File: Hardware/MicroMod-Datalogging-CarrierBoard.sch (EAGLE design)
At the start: 75 parts, among them J11 microSD, J12 SPI, J14 I2C, J2 JTAG, J3 QWIIC_RIGHT_ANGLE, J5 UART, J6 MICROMOD-2222-C, J8 Dedicated, U1 3.3V, U2 MCP73831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

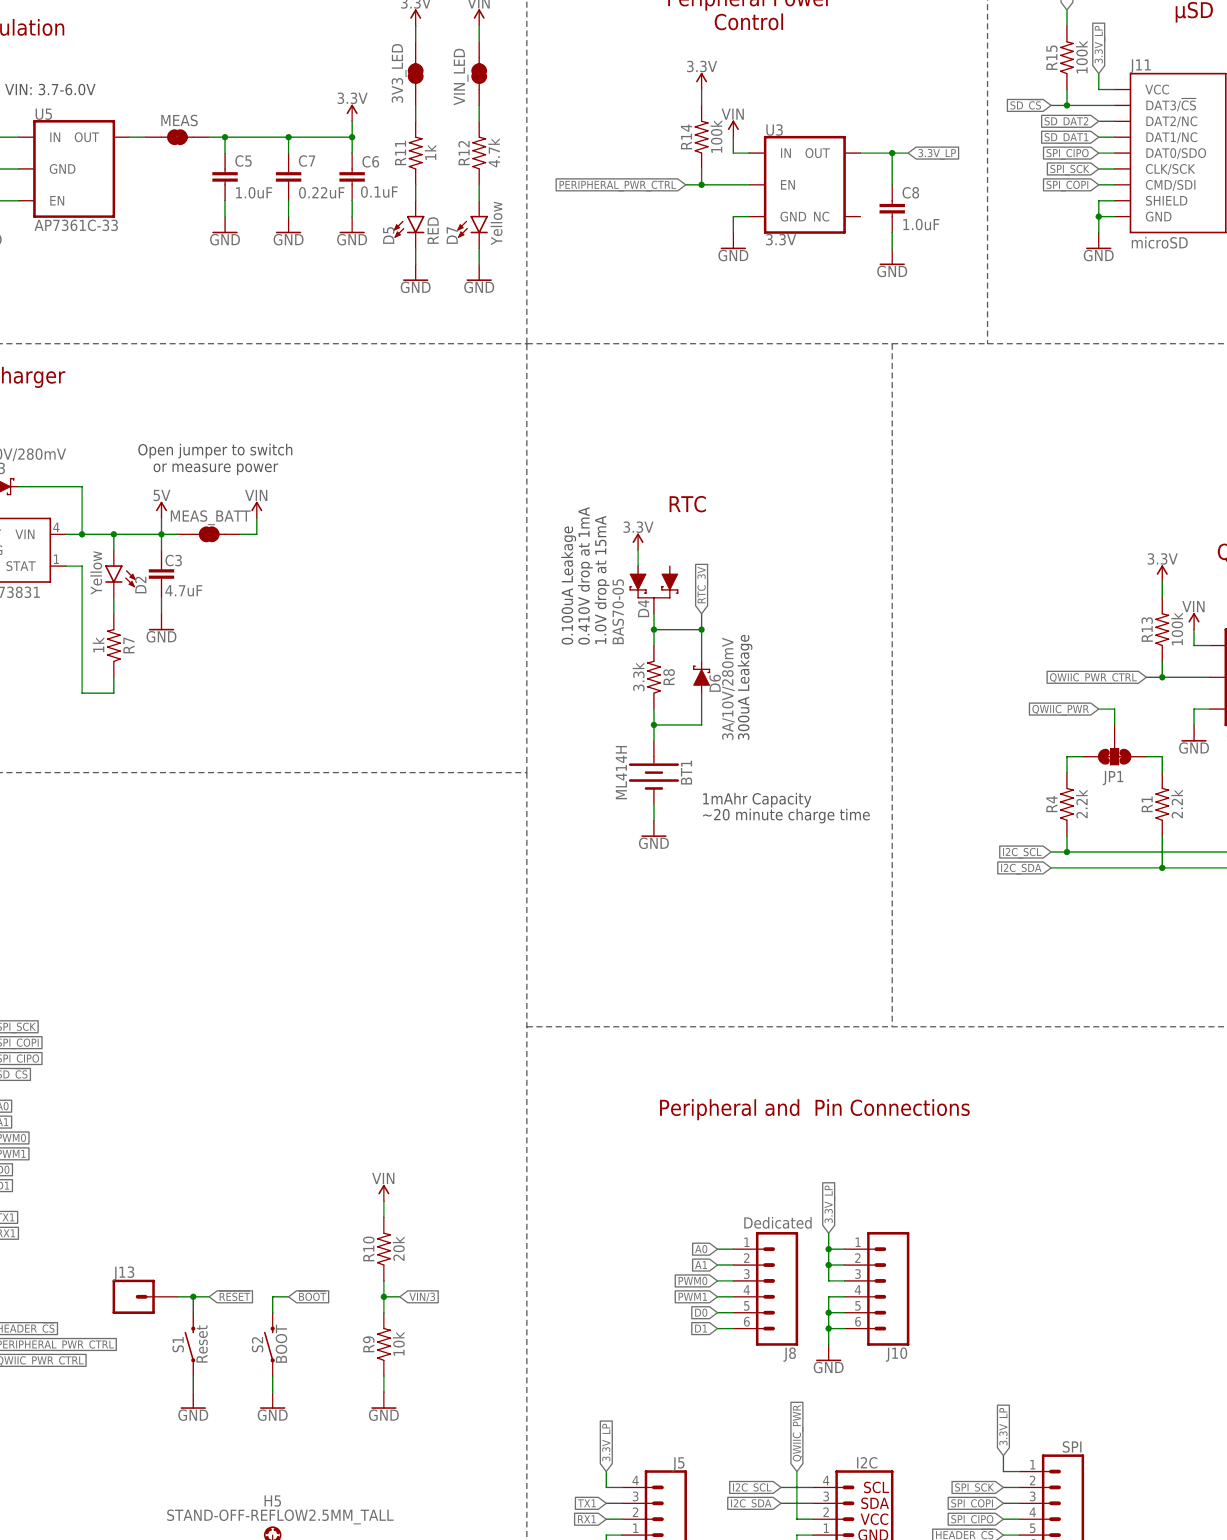
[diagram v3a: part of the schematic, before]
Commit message: Change SD to pure SPI connection.
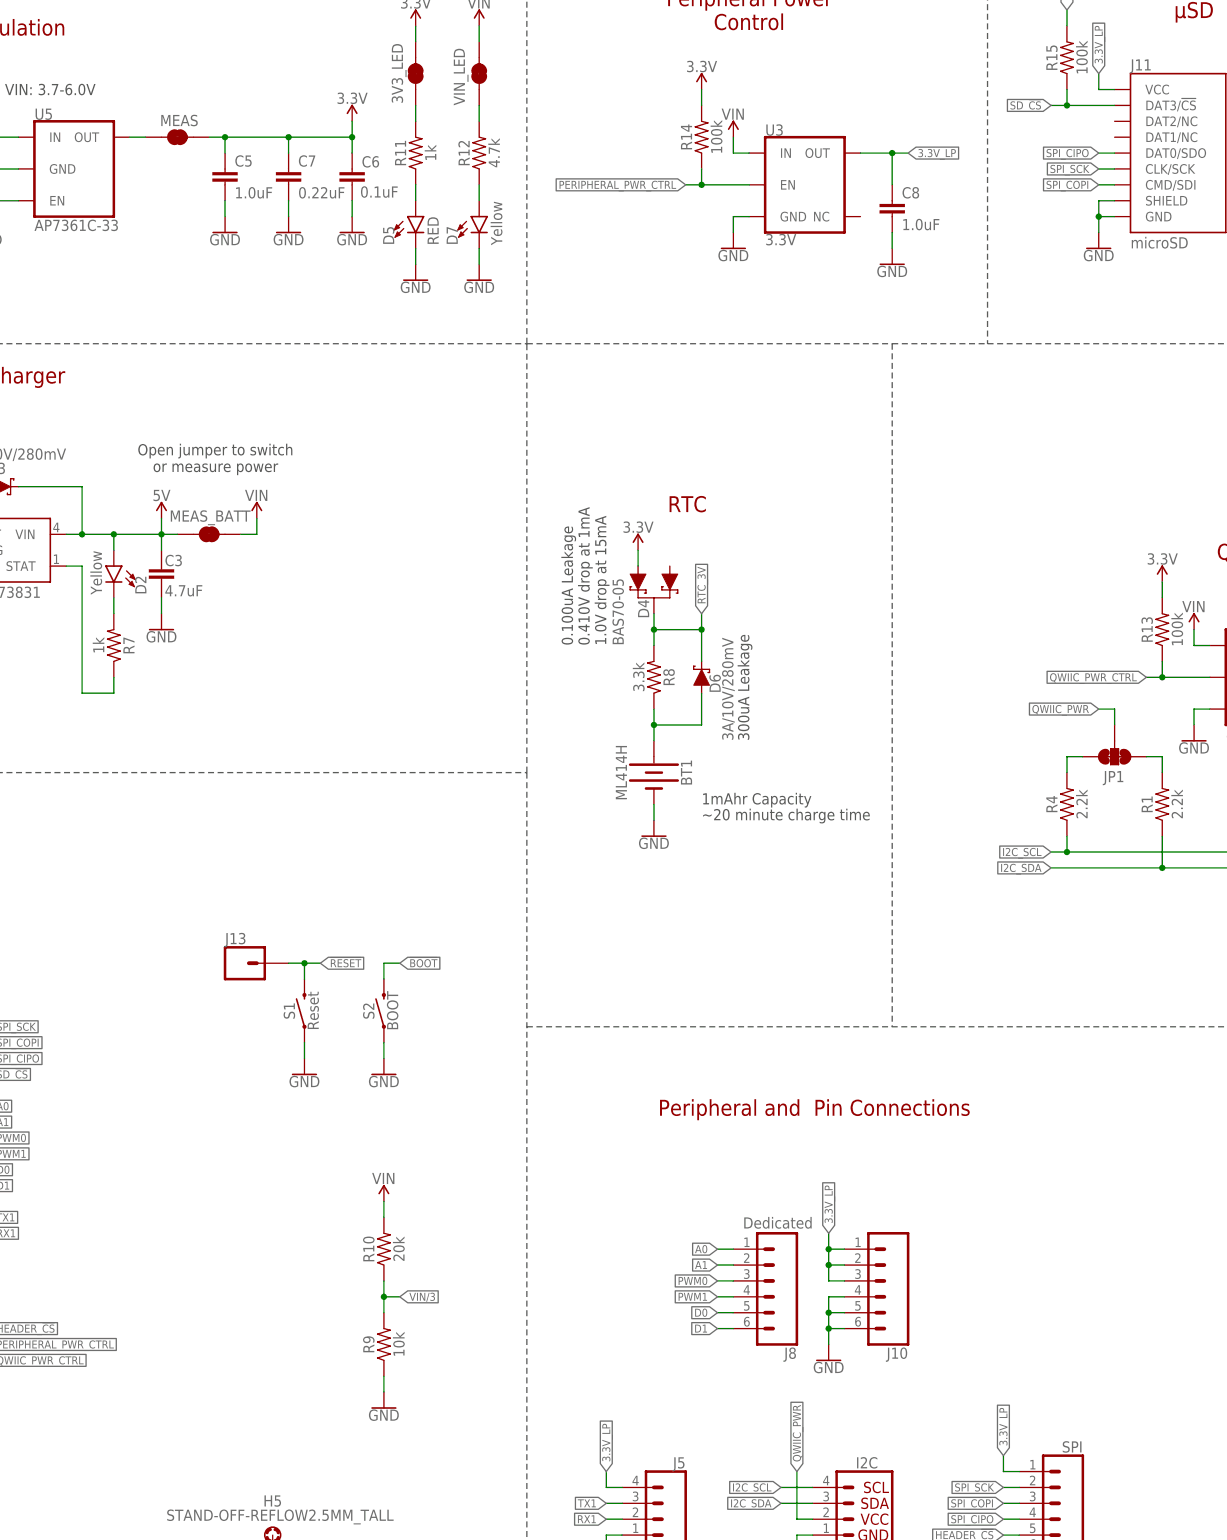
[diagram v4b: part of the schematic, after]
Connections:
- removed net SD_DAT1: J11.DAT1/NC
- removed net SD_DAT2: J11.DAT2/NC
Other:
- moved on the sheet: J13, S1, S2
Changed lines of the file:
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@@
 <?xml version="1.0" encoding="utf-8"?>
 <!DOCTYPE eagle SYSTEM "eagle.dtd">
-<eagle version="9.5.2">
+<eagle version="9.6.2">
 <drawing>
 <settings>
@@
 <attribute name="VALUE" x="255.524" y="142.24" size="1.778" layer="96" font="vector" rot="R90" align="top-center"/>
 </instance>
-<instance part="S1" gate="G$1" x="114.3" y="55.88" smashed="yes" rot="R90">
-<attribute name="NAME" x="112.776" y="55.88" size="1.778" layer="95" font="vector" rot="R90" align="bottom-center"/>
-<attribute name="VALUE" x="114.808" y="55.88" size="1.778" layer="96" font="vector" rot="R90" align="top-center"/>
+<instance part="S1" gate="G$1" x="132.08" y="109.22" smashed="yes" rot="R90">
+<attribute name="NAME" x="130.556" y="109.22" size="1.778" layer="95" font="vector" rot="R90" align="bottom-center"/>
+<attribute name="VALUE" x="132.588" y="109.22" size="1.778" layer="96" font="vector" rot="R90" align="top-center"/>
 </instance>
 <instance part="C1" gate="G$1" x="45.72" y="241.3" smashed="yes" rot="MR0">
@@
 <attribute name="VALUE" x="144.78" y="45.466" size="1.778" layer="96" align="top-center"/>
 </instance>
-<instance part="GND5" gate="1" x="114.3" y="45.72" smashed="yes">
-<attribute name="VALUE" x="114.3" y="45.466" size="1.778" layer="96" align="top-center"/>
+<instance part="GND5" gate="1" x="132.08" y="99.06" smashed="yes">
+<attribute name="VALUE" x="132.08" y="98.806" size="1.778" layer="96" align="top-center"/>
 </instance>
 <instance part="SUPPLY17" gate="G$1" x="27.94" y="251.46" smashed="yes">
@@
 <attribute name="VALUE" x="45.72" y="233.426" size="1.778" layer="96" align="top-center"/>
 </instance>
-<instance part="S2" gate="G$1" x="127" y="55.88" smashed="yes" rot="R90">
-<attribute name="NAME" x="125.476" y="55.88" size="1.778" layer="95" font="vector" rot="R90" align="bottom-center"/>
-<attribute name="VALUE" x="127.508" y="55.88" size="1.778" layer="96" font="vector" rot="R90" align="top-center"/>
-</instance>
-<instance part="GND15" gate="1" x="127" y="45.72" smashed="yes" rot="MR0">
-<attribute name="VALUE" x="127" y="45.466" size="1.778" layer="96" rot="MR0" align="top-center"/>
+<instance part="S2" gate="G$1" x="144.78" y="109.22" smashed="yes" rot="R90">
+<attribute name="NAME" x="143.256" y="109.22" size="1.778" layer="95" font="vector" rot="R90" align="bottom-center"/>
+<attribute name="VALUE" x="145.288" y="109.22" size="1.778" layer="96" font="vector" rot="R90" align="top-center"/>
+</instance>
+<instance part="GND15" gate="1" x="144.78" y="99.06" smashed="yes" rot="MR0">
+<attribute name="VALUE" x="144.78" y="98.806" size="1.778" layer="96" rot="MR0" align="top-center"/>
 </instance>
 <instance part="J8" gate="G$1" x="205.74" y="66.04" smashed="yes" rot="R180">
@@
 <attribute name="VALUE" x="183.134" y="167.64" size="1.778" layer="96" font="vector" rot="MR90" align="top-left"/>
 </instance>
-<instance part="J13" gate="G$1" x="104.14" y="63.5" smashed="yes">
-<attribute name="VALUE" x="101.6" y="58.674" size="1.778" layer="96" font="vector"/>
-<attribute name="NAME" x="101.6" y="66.548" size="1.778" layer="95" font="vector"/>
+<instance part="J13" gate="G$1" x="121.92" y="116.84" smashed="yes">
+<attribute name="VALUE" x="119.38" y="112.014" size="1.778" layer="96" font="vector"/>
+<attribute name="NAME" x="119.38" y="119.888" size="1.778" layer="95" font="vector"/>
 </instance>
 <instance part="3V3_LED" gate="G$1" x="149.86" y="259.08" smashed="yes" rot="R90">
@@
 </busses>
 <nets>
-<net name="SD_DAT1" class="0">
-<segment>
-<wire x1="261.62" y1="248.92" x2="259.08" y2="248.92" width="0.1524" layer="91"/>
-<label x="259.08" y="248.92" size="1.27" layer="95" rot="R180" xref="yes"/>
-<pinref part="J11" gate="G$1" pin="DAT1/NC"/>
-</segment>
-</net>
 <net name="SPI_SCK" class="0">
 <segment>
@@
 <wire x1="78.74" y1="99.06" x2="81.28" y2="99.06" width="0.1524" layer="91"/>
 <label x="81.28" y="99.06" size="1.27" layer="95" xref="yes"/>
-</segment>
-</net>
-<net name="SD_DAT2" class="0">
-<segment>
-<wire x1="261.62" y1="251.46" x2="259.08" y2="251.46" width="0.1524" layer="91"/>
-<label x="259.08" y="251.46" size="1.27" layer="95" rot="R180" xref="yes"/>
-<pinref part="J11" gate="G$1" pin="DAT2/NC"/>
 </segment>
 </net>
@@
 </segment>
 <segment>
-<wire x1="114.3" y1="50.8" x2="114.3" y2="48.26" width="0.1524" layer="91"/>
+<wire x1="132.08" y1="104.14" x2="132.08" y2="101.6" width="0.1524" layer="91"/>
 <pinref part="S1" gate="G$1" pin="1"/>
 <pinref part="GND5" gate="1" pin="GND"/>
@@
 <pinref part="S2" gate="G$1" pin="1"/>
 <pinref part="GND15" gate="1" pin="GND"/>
-<wire x1="127" y1="48.26" x2="127" y2="50.8" width="0.1524" layer="91"/>
+<wire x1="144.78" y1="101.6" x2="144.78" y2="104.14" width="0.1524" layer="91"/>
 </segment>
 <segment>
@@
 </segment>
 <segment>
-<wire x1="116.84" y1="63.5" x2="114.3" y2="63.5" width="0.1524" layer="91"/>
-<wire x1="114.3" y1="60.96" x2="114.3" y2="63.5" width="0.1524" layer="91"/>
+<wire x1="134.62" y1="116.84" x2="132.08" y2="116.84" width="0.1524" layer="91"/>
+<wire x1="132.08" y1="114.3" x2="132.08" y2="116.84" width="0.1524" layer="91"/>
 <pinref part="S1" gate="G$1" pin="2"/>
-<label x="116.84" y="63.5" size="1.27" layer="95" xref="yes"/>
-<wire x1="114.3" y1="63.5" x2="111.76" y2="63.5" width="0.1524" layer="91"/>
-<junction x="114.3" y="63.5"/>
+<label x="134.62" y="116.84" size="1.27" layer="95" xref="yes"/>
+<wire x1="132.08" y1="116.84" x2="129.54" y2="116.84" width="0.1524" layer="91"/>
+<junction x="132.08" y="116.84"/>
 <pinref part="J13" gate="G$1" pin="1"/>
 </segment>
@@
 <segment>
 <pinref part="S2" gate="G$1" pin="2"/>
-<wire x1="127" y1="60.96" x2="127" y2="63.5" width="0.1524" layer="91"/>
-<wire x1="127" y1="63.5" x2="129.54" y2="63.5" width="0.1524" layer="91"/>
-<label x="129.54" y="63.5" size="1.27" layer="95" xref="yes"/>
-</segment>
-</net>
+<wire x1="144.78" y1="114.3" x2="144.78" y2="116.84" width="0.1524" layer="91"/>
+<wire x1="144.78" y1="116.84" x2="147.32" y2="116.84" width="0.1524" layer="91"/>
+<label x="147.32" y="116.84" size="1.27" layer="95" xref="yes"/>
+</segment>
+</net>
